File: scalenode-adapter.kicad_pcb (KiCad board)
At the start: 4 copper layers, 96 x 40 mm, 167 parts, among them IC1 FT2232D, IC2 TPD8S009DSMR, J1 QTE-020-04-L-D-A, J10 3-794680-8, J11 1-794610-1, J12 1-794610-1, J13 1-794610-1, J14 1-794610-1, J15 794617-8, J16 1-794610-1, J17 1-794610-1, J18 1-794610-1, J19 1-794610-1, J2 0022232041, J20 8-188275-2, J3 614004185023, J4 WE_629105150521, J5 614004185023, J6 614004185023, J7 QTE-020-04-L-D-A, J8 WE_629105150521, J9 WE_685119136923, Q1 FDC6330L, Q2 FDC6330L, Q3 FDC6330L, U1 PCT2075GVX, U2 PAC1934T-I_JQ, U3 USB2514B-I_M2, U4 TPS2024DR, U5 TPS2024DR, U6 TPS2024DR, U7 FT230XS-R, Y1 7C-24.000MBB-T, Y2 MQ-6.000-12-30_30_

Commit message: Update naming convention
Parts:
- 3V1, 5V1, GND1, GND2: footprint antartix-arty-controller-footprints:Testpoint_smd_1mm -> scalenode-adapter-footprints:Testpoint_smd_1mm
- C1, C13, C15, C16, C17, C19, C2, C20, C21, C23, C24, C25, C26, C27, C28, C29, C3, C31, C32, C33, C34, C35, C36, C4, C41, C42, C43, C44, C45, C46, C47, C48, C49, C5, C50, C51, C52, C53, C55, C56, C57, C58, C6, C7, C8, C9: footprint antartix-arty-controller-footprints:0402-cap -> scalenode-adapter-footprints:0402-cap
- C10, C11, C12, C37, C38, C39, C54: footprint antartix-arty-controller-footprints:0603-cap -> scalenode-adapter-footprints:0603-cap
- C14, C18, C22, C30, C40: footprint antartix-arty-controller-footprints:KEMET_D -> scalenode-adapter-footprints:KEMET_D
- D1, D2, D3, D4, D5, D6, D8, D9: footprint antartix-arty-controller-footprints:LED_0603 -> scalenode-adapter-footprints:LED_0603
- D10, D7: footprint antartix-arty-controller-footprints:SOT-3 -> scalenode-adapter-footprints:SOT-3
- FB1, FB2, R3, R37, R4: footprint antartix-arty-controller-footprints:0805-res -> scalenode-adapter-footprints:0805-res
- IC1: footprint antartix-arty-controller-footprints:LQFP-48_7x7mm -> scalenode-adapter-footprints:LQFP-48_7x7mm
- IC2: footprint antartix-arty-controller-footprints:R-PDSO-N15 -> scalenode-adapter-footprints:R-PDSO-N15
- J1, J7: footprint antartix-arty-controller-footprints:QTE-020-04-L-D-A -> scalenode-adapter-footprints:QTE-020-04-L-D-A
- J10: footprint antartix-arty-controller-footprints:3-794680-8 -> scalenode-adapter-footprints:3-794680-8
- J11, J12, J13, J14, J16, J17, J18, J19: footprint antartix-arty-controller-footprints:1-794610-1 -> scalenode-adapter-footprints:1-794610-1
- J15: footprint antartix-arty-controller-footprints:3-794617-8 -> scalenode-adapter-footprints:3-794617-8
- J2: footprint antartix-arty-controller-footprints:PinHeader_1x4_P2.54mm_Drill1.02mm -> scalenode-adapter-footprints:PinHeader_1x4_P2.54mm_Drill1.02mm
- J20: footprint antartix-arty-controller-footprints:8-188275-2 -> scalenode-adapter-footprints:8-188275-2
- J4, J8: footprint antartix-arty-controller-footprints:USB_Micro_B_Female_629105150521 -> scalenode-adapter-footprints:USB_Micro_B_Female_629105150521
- J9: footprint antartix-arty-controller-footprints:WE_685119136923 -> scalenode-adapter-footprints:WE_685119136923
- N1: footprint antartix-arty-controller-footprints:antmicro-logo_scaled_15mm -> scalenode-adapter-footprints:antmicro-logo_scaled_15mm
- N2: footprint antartix-arty-controller-footprints:oshw-logo -> scalenode-adapter-footprints:oshw-logo
- Q1, Q2, Q3: footprint antartix-arty-controller-footprints:FDC6330L -> scalenode-adapter-footprints:FDC6330L
- R1, R10, R11, R12, R13, R14, R17, R18, R19, R2, R20, R23, R24, R25, R26, R27, R28, R29, R30, R31, R32, R33, R34, R35, R36, R38, R39, R40, R41, R42, R43, R44, R45, R46, R47, R48, R49, R5, R50, R51, R52, R53, R54, R55, R56, R57, R6, R7, R8, R9: footprint antartix-arty-controller-footprints:0402-res -> scalenode-adapter-footprints:0402-res
- R15, R16, R21, R22: footprint antartix-arty-controller-footprints:1206-res -> scalenode-adapter-footprints:1206-res
- U1: footprint antartix-arty-controller-footprints:SOT95P275X110-6N -> scalenode-adapter-footprints:SOT95P275X110-6N
- U2: footprint antartix-arty-controller-footprints:QFN65P400X400X55-17N -> scalenode-adapter-footprints:QFN65P400X400X55-17N
- U3: footprint antartix-arty-controller-footprints:QFN50P600X600X100-37N -> scalenode-adapter-footprints:QFN50P600X600X100-37N
- U4, U5, U6: footprint antartix-arty-controller-footprints:SOIC-8_W3.9mm -> scalenode-adapter-footprints:SOIC-8_W3.9mm
- U7: footprint antartix-arty-controller-footprints:SSOP-16_W3.90mm -> scalenode-adapter-footprints:SSOP-16_W3.90mm
- Y1: footprint antartix-arty-controller-footprints:7C-24.000MBB-T -> scalenode-adapter-footprints:7C-24.000MBB-T
- Y2: footprint antartix-arty-controller-footprints:Crystal_5x7mm -> scalenode-adapter-footprints:Crystal_5x7mm

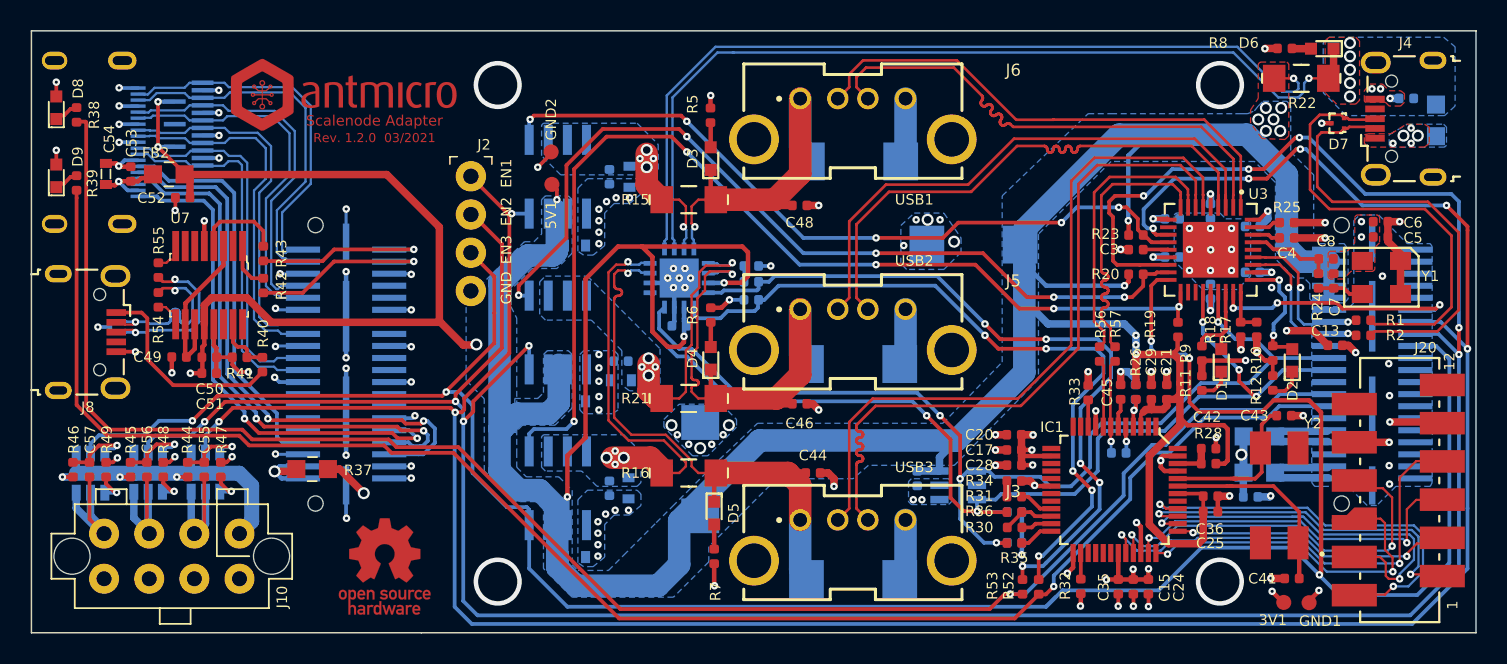
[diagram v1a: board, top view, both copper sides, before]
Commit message: Connect EP of U2 to GND to resolve DRC
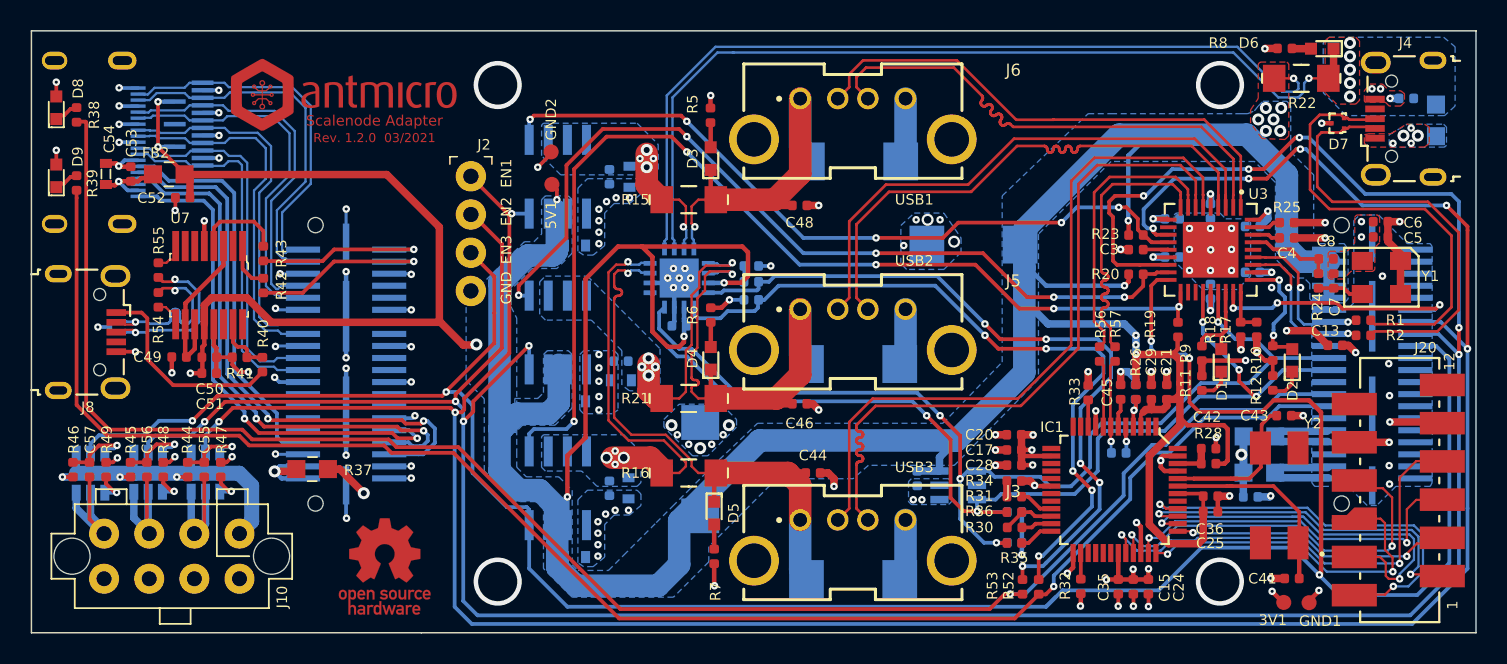
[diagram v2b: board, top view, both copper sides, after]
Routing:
- net Net-(C43-Pad1): track 10.4 -> 12.8 mm
